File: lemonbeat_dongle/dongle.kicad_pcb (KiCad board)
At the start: 4 copper layers, 50 x 20 mm, 71 parts, among them J201 USB_A, J202 Prog, J203 u.FL, J301 SMA, SW201 SW_Push, U201 nRF52840, U301 Si4467, Y201 32MHz, Y202 32.768kHz, Y301 26MHz

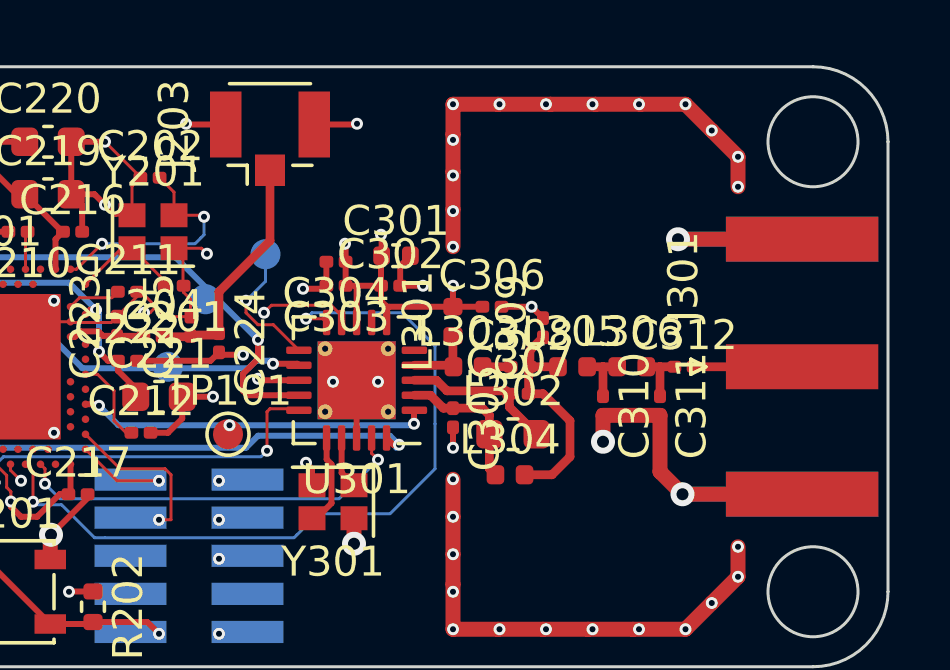
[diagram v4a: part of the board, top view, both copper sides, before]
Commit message: dongle: better GND connection for RF connectors
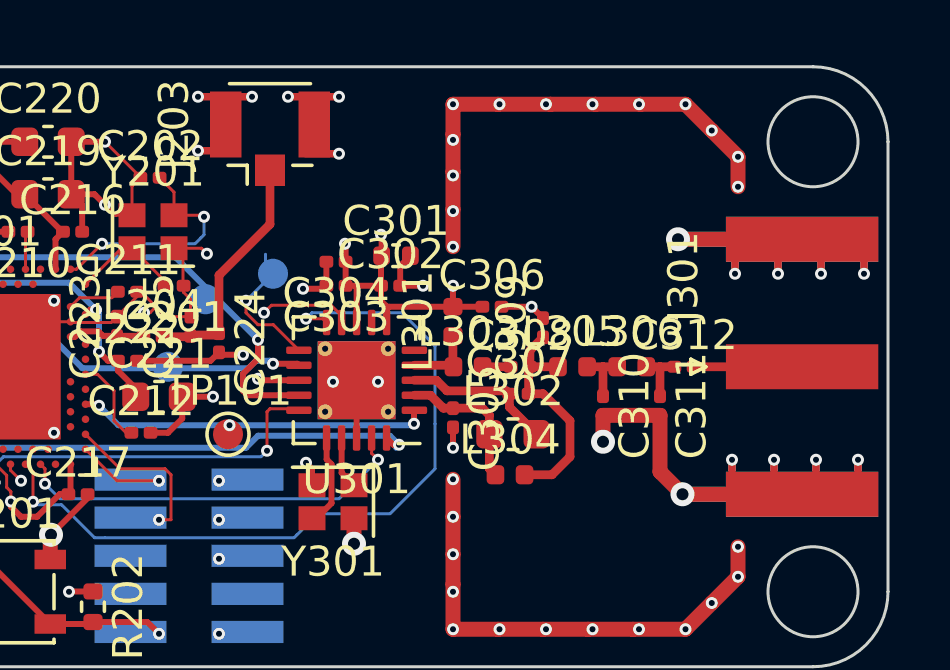
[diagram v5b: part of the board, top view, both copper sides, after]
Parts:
- moved TP106 0.70 mm to (140.0, 100.9)
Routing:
- net GND: track 122.8 -> 139.3 mm, vias 60 -> 72

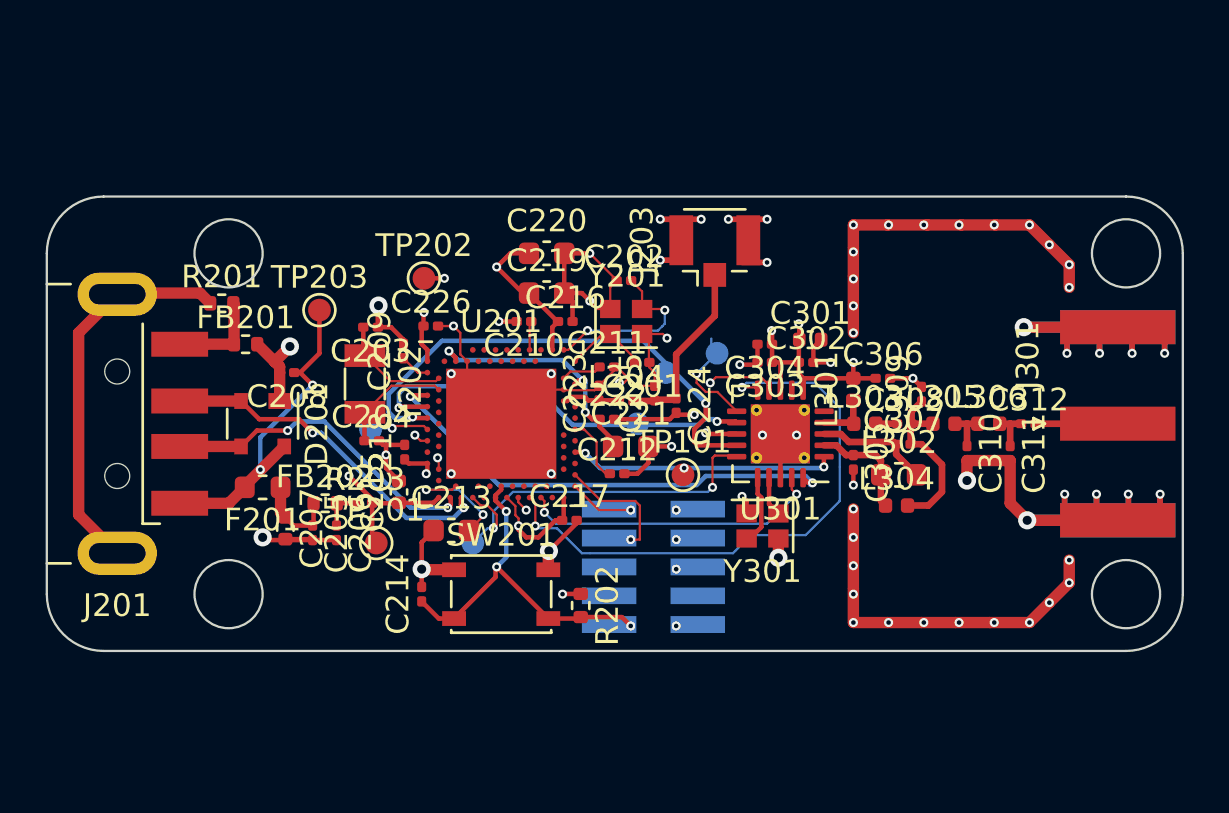
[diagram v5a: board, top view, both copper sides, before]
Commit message: dongle: improve USB routing & fix DRC errors
USB 2.0 impedance should be 90 Ω and there should be no skew in the
wires (different length). This is likely irrelevant at 12 Mbps, but
still fixed now :-)

For details on routing of differential pairs in KiCAD, see
https://www.digikey.ch/en/maker/projects/how-to-route-differential-pairs-in-kicad-for-usb/45b99011f5d34879ae1831dce1f13e93

This commit also fixes all DRC errors.
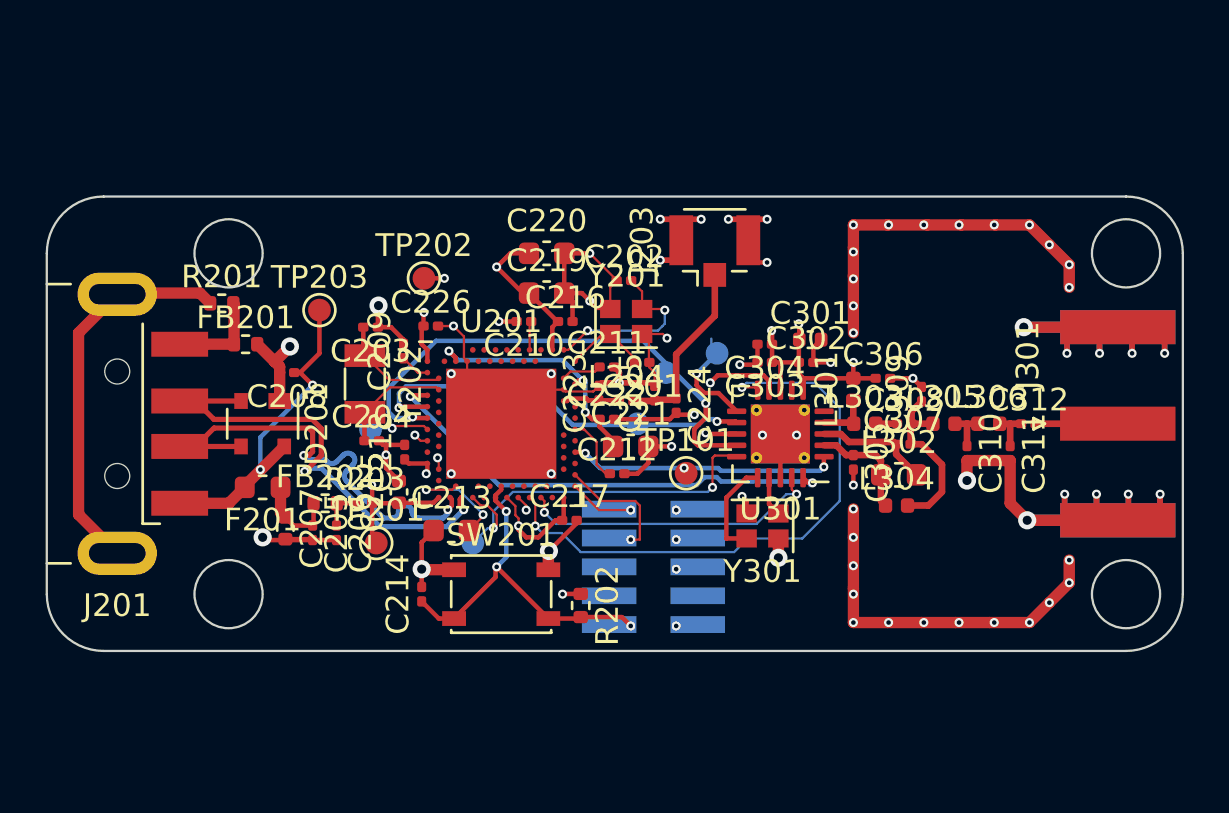
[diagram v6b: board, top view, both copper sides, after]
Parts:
- moved TP101 0.16 mm to (138.6, 106.2)
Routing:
- net /MCU/D_N: track 14.3 -> 20.7 mm
- net /MCU/D_P: track 15.3 -> 20.7 mm
- net /MCU/VBUS_nRF: track 11.2 -> 9.58 mm
- net Net-(U301-Pad16): track 3.10 -> 4.43 mm
- net GND: track 139.3 -> 138.5 mm

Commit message: dongle: fix all non-silkscreen DRC warnings
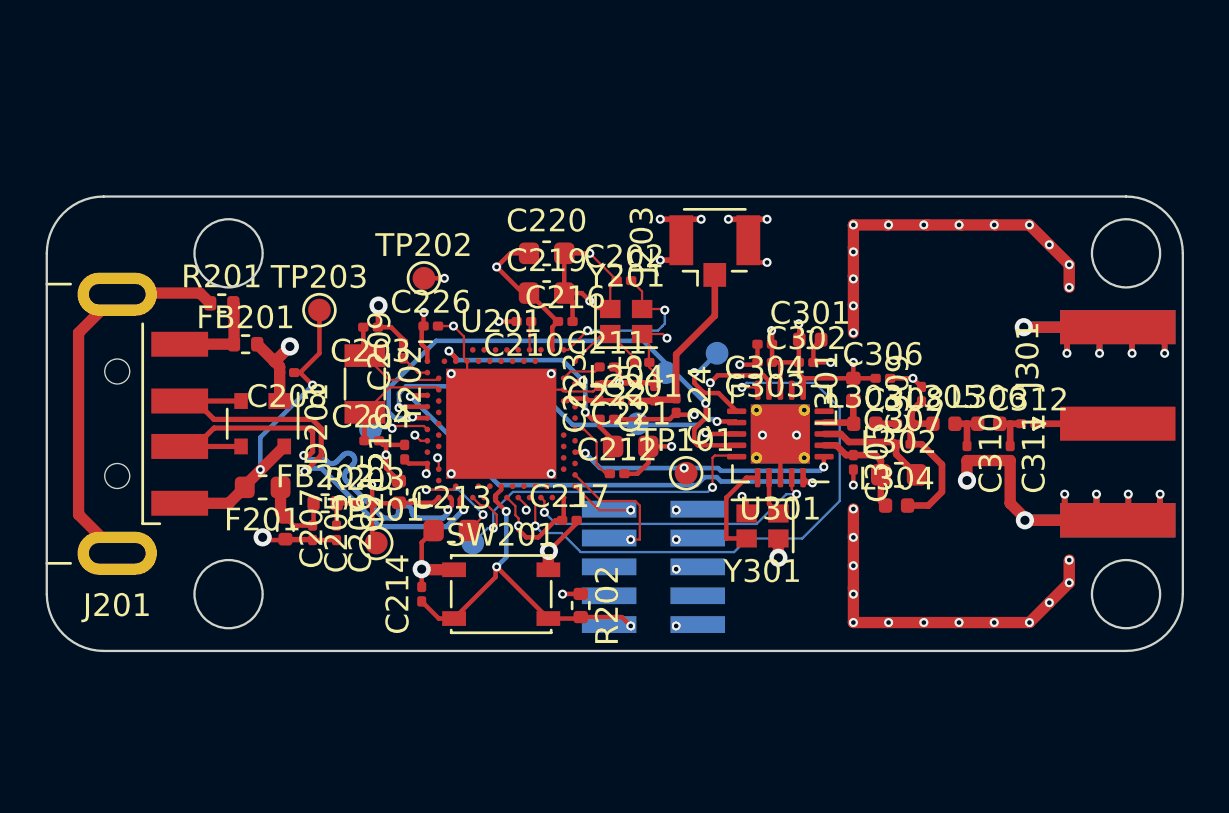
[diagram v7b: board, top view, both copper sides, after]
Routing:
- net /MCU/P1.09: track 19.2 -> 18.3 mm
- net Net-(C204-Pad1): track 5.57 -> 5.01 mm

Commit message: dongle: add smart logo
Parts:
- added G1: smart logo, custom_library:smart_tulip_soldermask, F.Cu at (150.5, 98.8)
